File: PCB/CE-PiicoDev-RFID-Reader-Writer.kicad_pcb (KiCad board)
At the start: 2 copper layers, 25.4 x 52 mm, 63 parts, among them J1 , J2 , J3 Conn_01x06_Male, J4 Conn_01x01_Male, SW1 SW_DIP_x02, U1 MFRC522, Y1 27.12MHz 12pF

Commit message: Rename Project
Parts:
- moved R7 3.93 mm to (93.1, 108.7)
- moved R6 3.15 mm to (94.9, 109.8), turned to 0 degrees
- moved R11 1.07 mm to (95.7, 106.1), turned to 270 degrees
- moved C11 0.13 mm to (99.1, 97.6)
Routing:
- net Net-(R7-Pad1): track 2.34 -> 20.4 mm, vias 1 -> 2
- net Net-(R6-Pad1): track 4.73 -> 19.0 mm
- net /SCL: track 48.9 -> 52.6 mm
- net +3V3: track 88.1 -> 91.5 mm
- net /SDA: track 45.9 -> 47.4 mm
- net Net-(R11-Pad1): track 2.80 -> 1.89 mm
- net GND: track 32.4 -> 33.3 mm, vias 15 -> 16
- net (no net): vias 0 -> 4
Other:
- board text added: "RFID Reader Writer"
- board text removed: "RFID Reader Writer MFRC522"

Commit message: Update
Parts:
- U1: footprint Package_DFN_QFN:VQFN-32-1EP_5x5mm_P0.5mm_EP3.1x3.1mm -> Package_DFN_QFN:VQFN-32-1EP_5x5mm_P0.5mm_EP3.1x3.1mm_ThermalVias
- moved TP3 7.77 mm to (95.7, 93.1)
- moved TP1 5.20 mm to (93.2, 98.9)
- moved C2 3.36 mm to (91.7, 95.3)
- moved Y1 2.24 mm to (92.9, 107.0), turned to 180 degrees
- moved TP2 1.61 mm to (93.4, 95.1)
- moved C13 1.32 mm to (94.8, 97.3)
- moved C3 1.32 mm to (93.8, 97.3)
- moved C11 1.32 mm to (98.0, 96.9)
- moved C12 1.32 mm to (99.9, 97.8)
- moved C14 1.32 mm to (100.9, 101.8)
- moved U1 1.32 mm to (97.3, 101.4)
- moved R9 1.32 mm to (101.0, 99.7)
- moved R4 1.28 mm to (92.2, 98.4)
- moved C4 1.25 mm to (92.7, 102.4)
- moved R7 1.19 mm to (93.5, 109.8), turned to 180 degrees
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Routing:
- net Net-(C1-Pad1): track 7.15 -> 12.3 mm
- net Net-(L1-Pad1): track 15.2 -> 11.3 mm
- net Net-(R7-Pad1): track 20.4 -> 16.7 mm
- net /INT: track 15.5 -> 19.2 mm
- net Net-(C2-Pad1): track 4.87 -> 1.43 mm
- net +3V3: track 91.5 -> 94.1 mm
- net Net-(R6-Pad1): track 19.0 -> 17.4 mm
- net Net-(C2-Pad2): track 9.46 -> 7.86 mm
- net GND: track 33.3 -> 34.8 mm, vias 16 -> 17
- net /SCL: track 52.6 -> 51.1 mm
- net /~RST: track 15.3 -> 16.7 mm
- net Net-(C3-Pad2): track 7.63 -> 6.82 mm
- net Net-(L2-Pad1): track 11.2 -> 10.6 mm, vias 2 -> 3
- net (no net): vias 4 -> 0

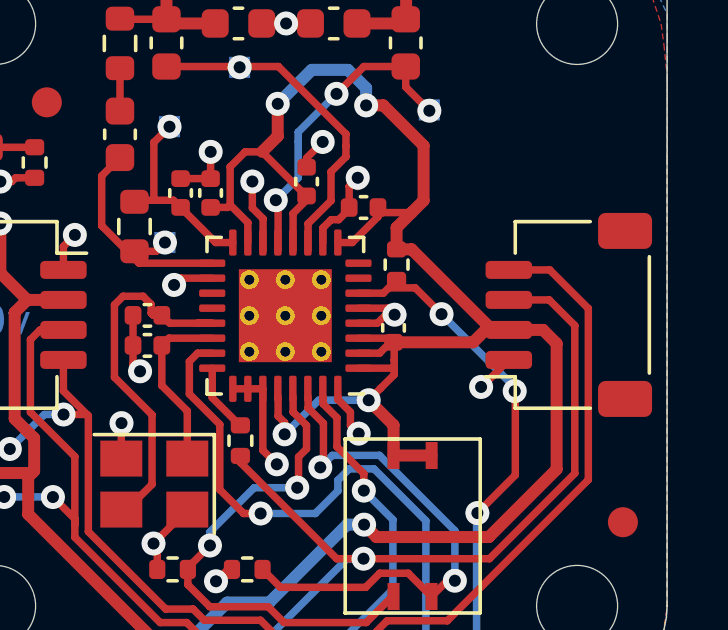
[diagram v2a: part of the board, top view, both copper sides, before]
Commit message: Move via from directly under C14
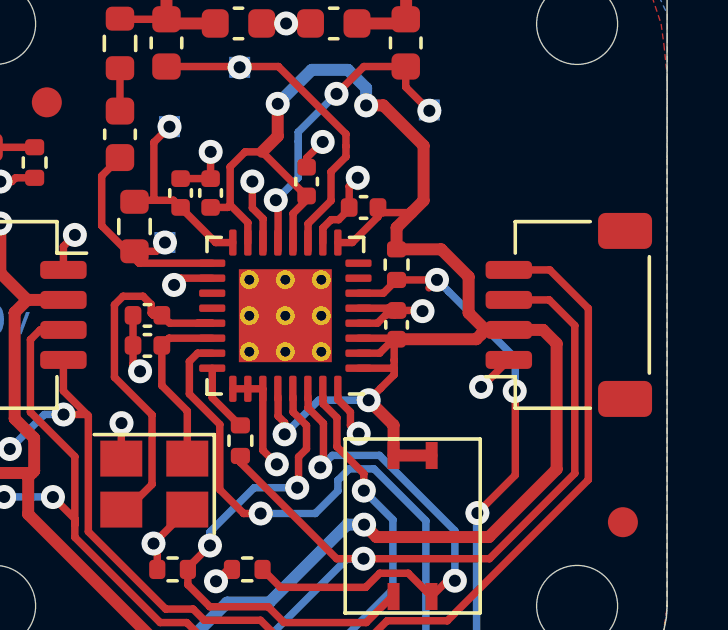
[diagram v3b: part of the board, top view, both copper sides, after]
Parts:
- moved C14 0.14 mm to (101.0, 101.7)
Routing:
- net GND: track 34.8 -> 35.6 mm
- net /~RST: track 16.7 -> 17.4 mm

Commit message: Update DIP Switch Footprint
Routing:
- net /SCL: track 51.1 -> 48.4 mm, vias 3 -> 5
- net +3V3: track 93.9 -> 94.8 mm
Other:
- board text added: "v04"
- board text removed: "v03"
